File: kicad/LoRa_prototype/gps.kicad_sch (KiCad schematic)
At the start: 6 parts, among them U5 L80-R

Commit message: Done schematic GPS block with 0 ERC errors (Milestone)
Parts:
- added D1: LED, symbol Device:LED
- added Q1, Q2: DTC143Z, symbol Transistor_BJT:DTC143Z
- added R13, R14, R15: 1K, symbol Device:R
- added R16: 5.6K, symbol Device:R
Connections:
- net GND: now also Q1.2 (E), Q2.2 (E), R16.1
- net VDD: now also D1.2 (A)
- net at U5.1 (RXD1): now also R14.1
- net at U5.10 (~{RESET}): now also Q2.3 (C)
- net at U5.2 (TXD1): now also R15.1, R16.2
- net at U5.6 (1PPS): now also Q1.1 (B)
- new net: D1.1 (K), R13.1
- new net: Q1.3 (C), R13.2
- new net GPS_RX: R14.2
- new net GPS_TX: R15.2
- new net GPS_~{RESET}: Q2.1 (B)
- no-connect marks 0 -> 3
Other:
- note added: "(2.8V)"
- note added: "(3.3V)"
- note added: "(from MCU)"
- note added: "(with internal PU)"
- moved on the sheet: C35, C36, C37, TP12, TP13, U5

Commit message: Copied and cleaned up USb charging circuit from WORK-CARE
1 ERC error
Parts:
- added TP17: GPS_TX, symbol Connector:TestPoint
- renumbered C37 to C38, C35 to C39, C36 to C40, D1 to D2, Q2 to Q1, Q1 to Q2, R16 to R19, R15 to R20, R14 to R21, R13 to R22, TP12 to TP15, TP13 to TP16, U5 to U6
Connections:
- net at R19.2, R20.1, U6.2 (TXD1): now also TP17.1
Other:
- note added: "(max 3.6V)"
- moved on the sheet: R20, R21

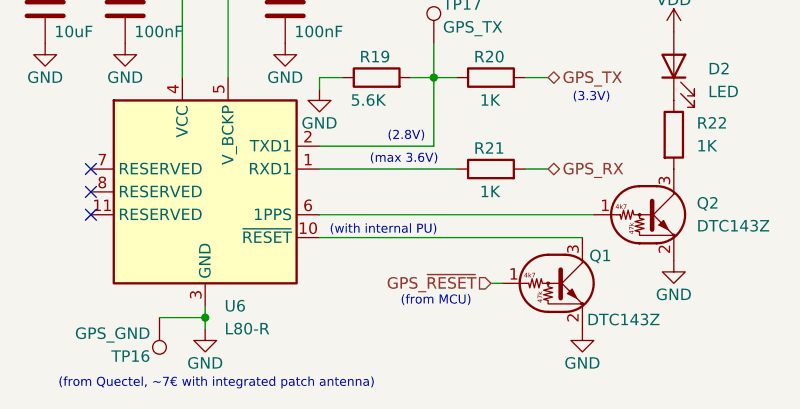
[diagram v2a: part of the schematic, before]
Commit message: Added I2C pullups for fuel guage
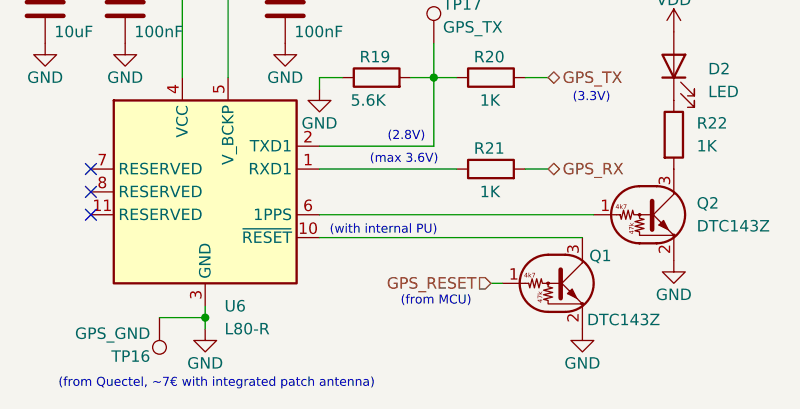
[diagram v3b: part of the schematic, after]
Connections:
- net GPS_~{RESET} renamed GPS_RESET
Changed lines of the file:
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@@
 		)
 	)
-	(hierarchical_label "GPS_~{RESET}"
+	(hierarchical_label "GPS_RESET"
 		(shape input)
 		(at 187.96 116.84 180)
